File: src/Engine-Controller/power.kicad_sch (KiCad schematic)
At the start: 45 parts, among them P1 EJ508A, P7 647676-2, U2 LM22672MRE-5.0_NOPB, U3 LMS8117AMP-3.3_NOPB, U6 TPS2115APWR

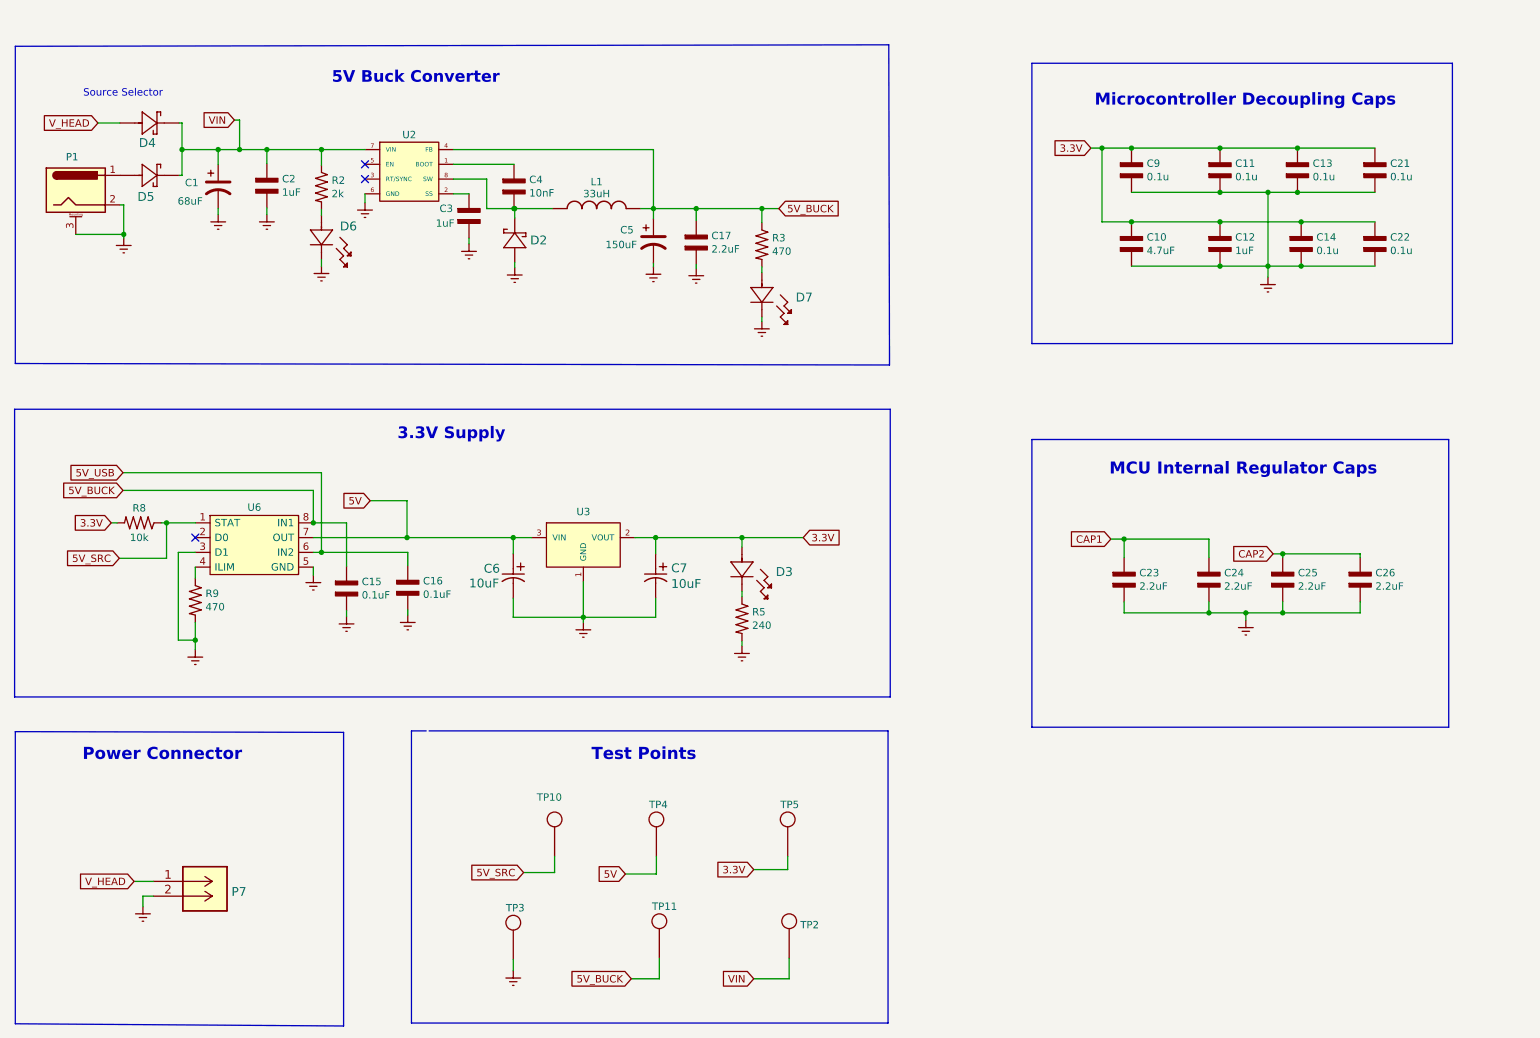
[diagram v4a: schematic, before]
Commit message: moved schematic components to 25 mil grid
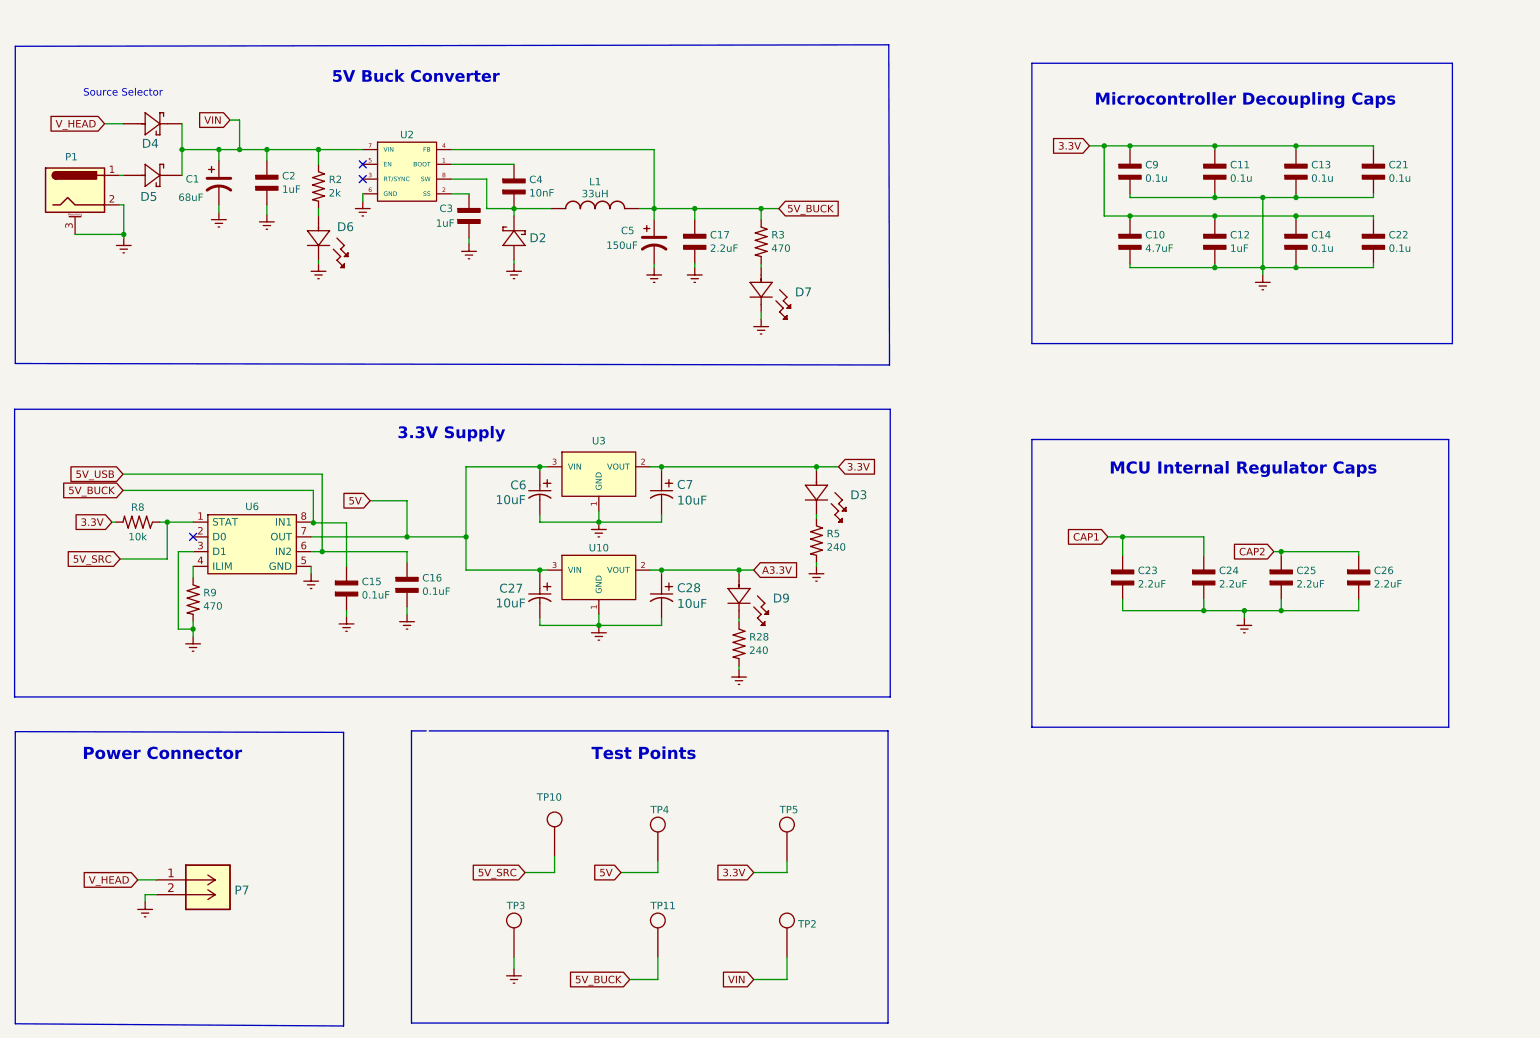
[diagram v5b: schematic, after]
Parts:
- added C27, C28: 10uF, Engine-Controller:CWR11HH106KB, symbol Engine-Controller:CWR11HH106KB
- added D9: SML-LX1206GC-TR, Engine-Controller:SML-LX1206GC-TR, symbol Engine-Controller:SML-LX1206GC-TR
- added R28: 240, Engine-Controller:RES_0603, symbol Engine-Controller:RES_0603
- added U10: LMS8117AMP-3.3_NOPB, Engine-Controller:SOT-223, symbol Engine-Controller:LMS8117AMP-3.3_NOPB
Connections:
- net 5V: now also C27.1, U10.3 (VIN)
- net Earth: now also C27.2, C28.2, R28.2, U10.1 (GND)
- new net: D9.1, R28.1
- new net A3.3V: C28.1, D9.2, U10.2 (VOUT)
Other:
- moved on the sheet: C1, C11, C12, C14, C16, C2, C24, C6, C7, D3, D4, D5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

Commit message: added schematic annotations
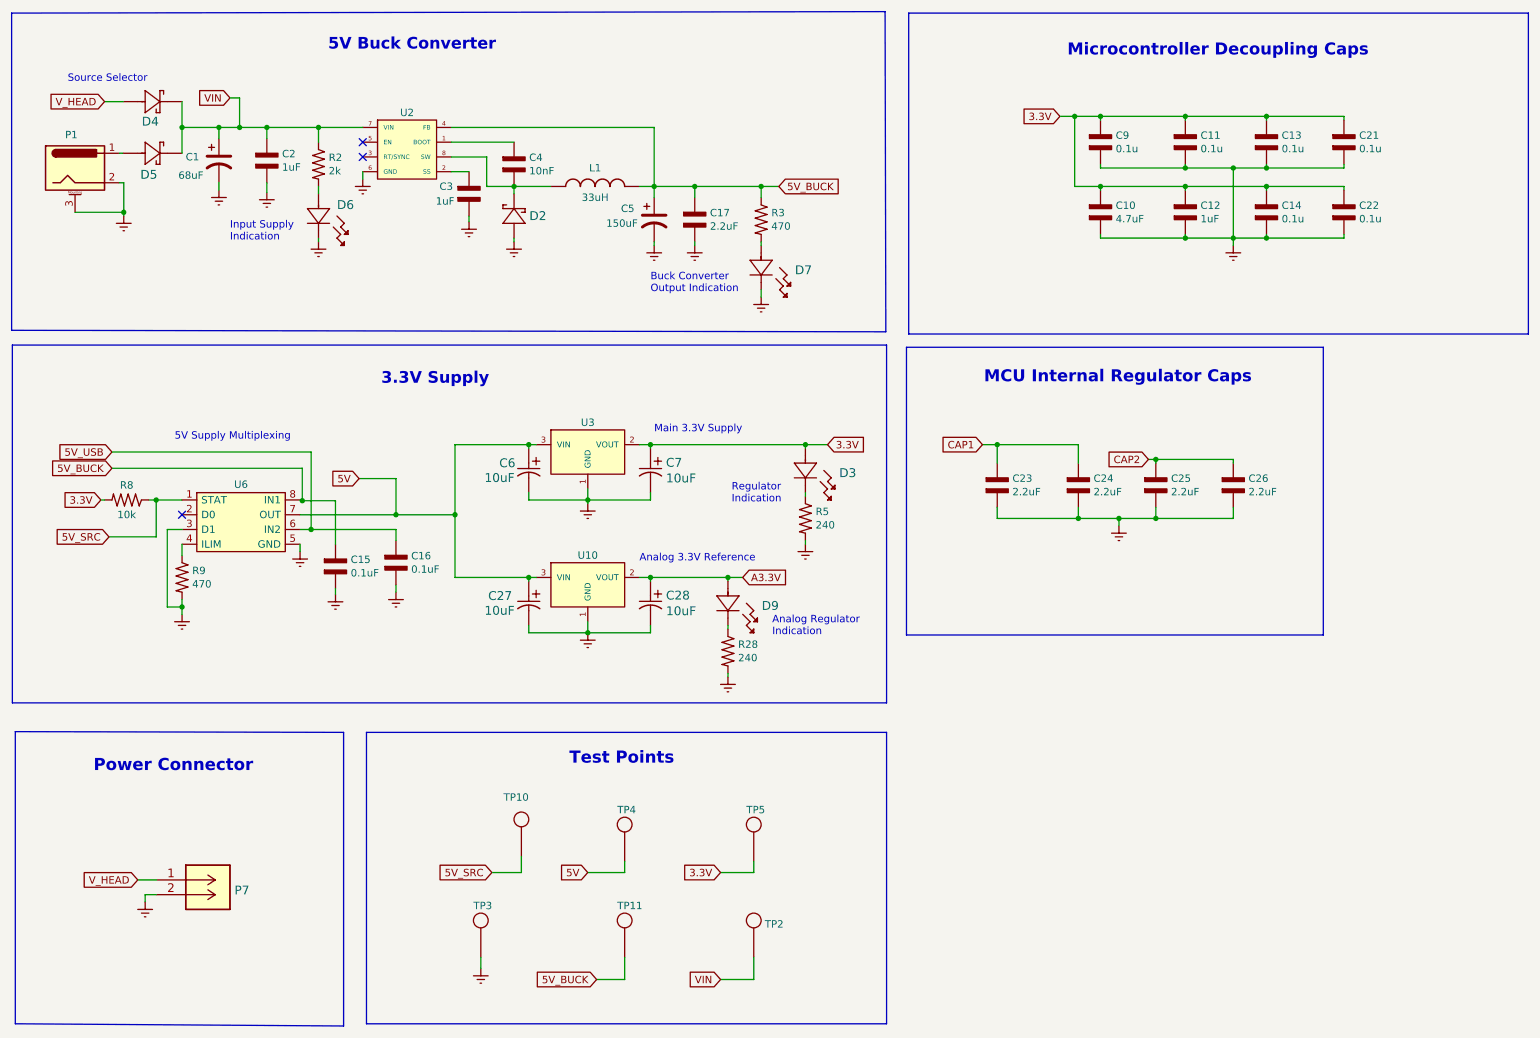
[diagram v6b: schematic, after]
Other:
- note added: "5V Supply Multiplexing"
- note added: "Analog 3.3V Reference"
- note added: "Analog Regulator Indication"
- note added: "Buck Converter Output Indication"
- note added: "Input Supply Indication"
- note added: "Main 3.3V Supply"
- note added: "Regulator Indication"
- moved on the sheet: C1, C10, C11, C12, C13, C14, C15, C16, C17, C2, C21, C22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

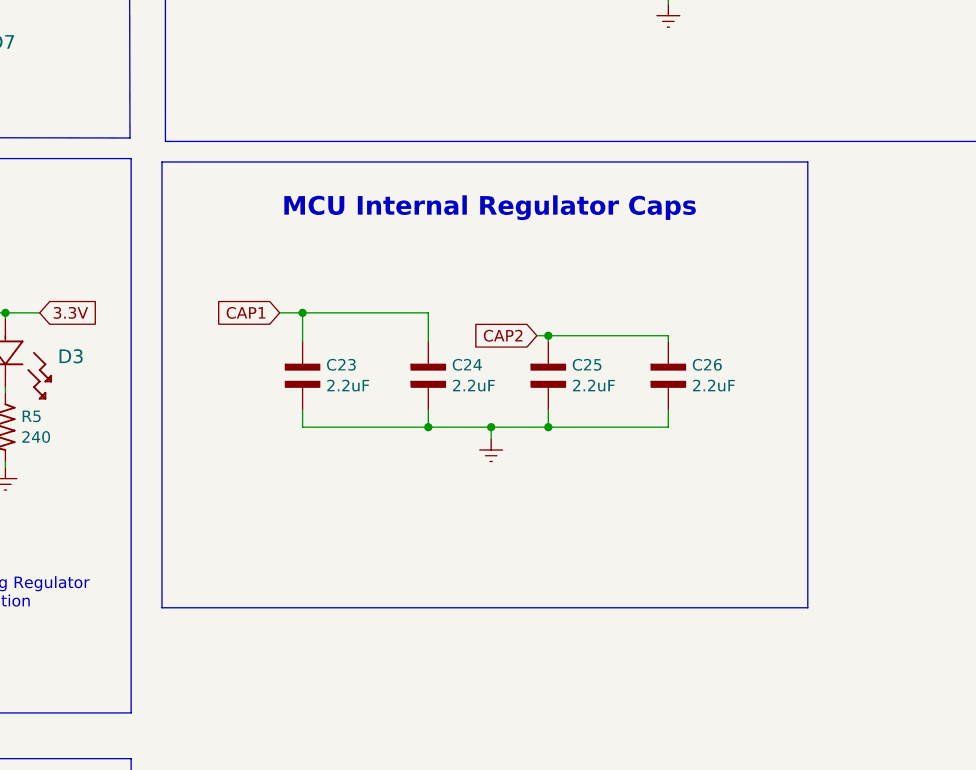
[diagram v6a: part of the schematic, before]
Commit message: added load cell amplifier to schematic
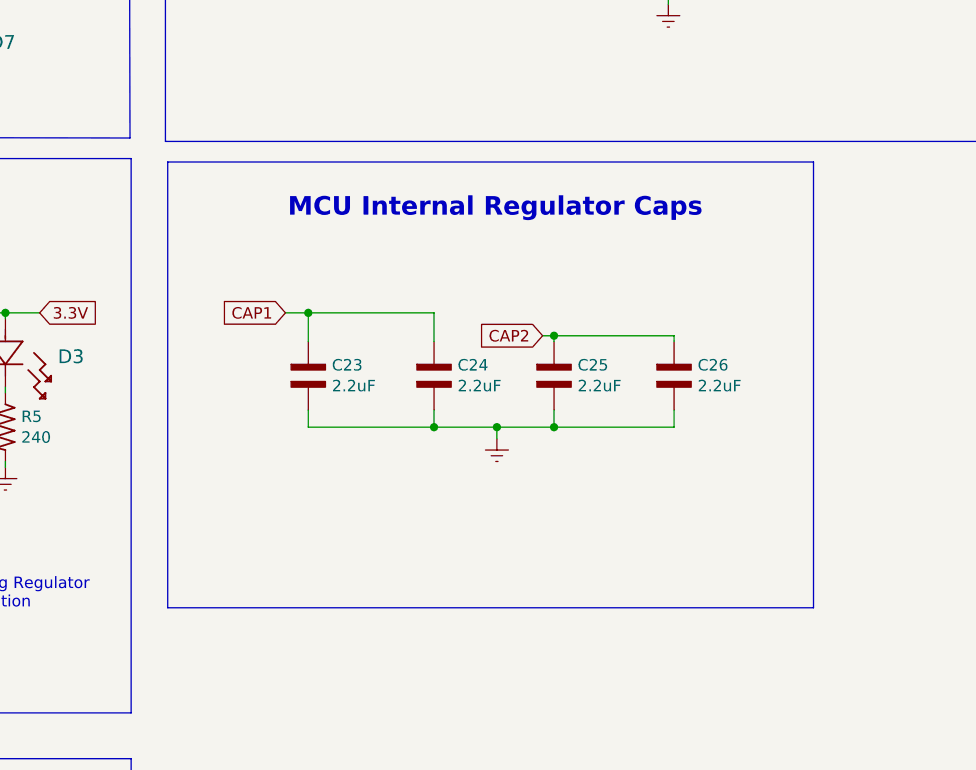
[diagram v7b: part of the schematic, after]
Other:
- moved on the sheet: C23, C24, C25, C26

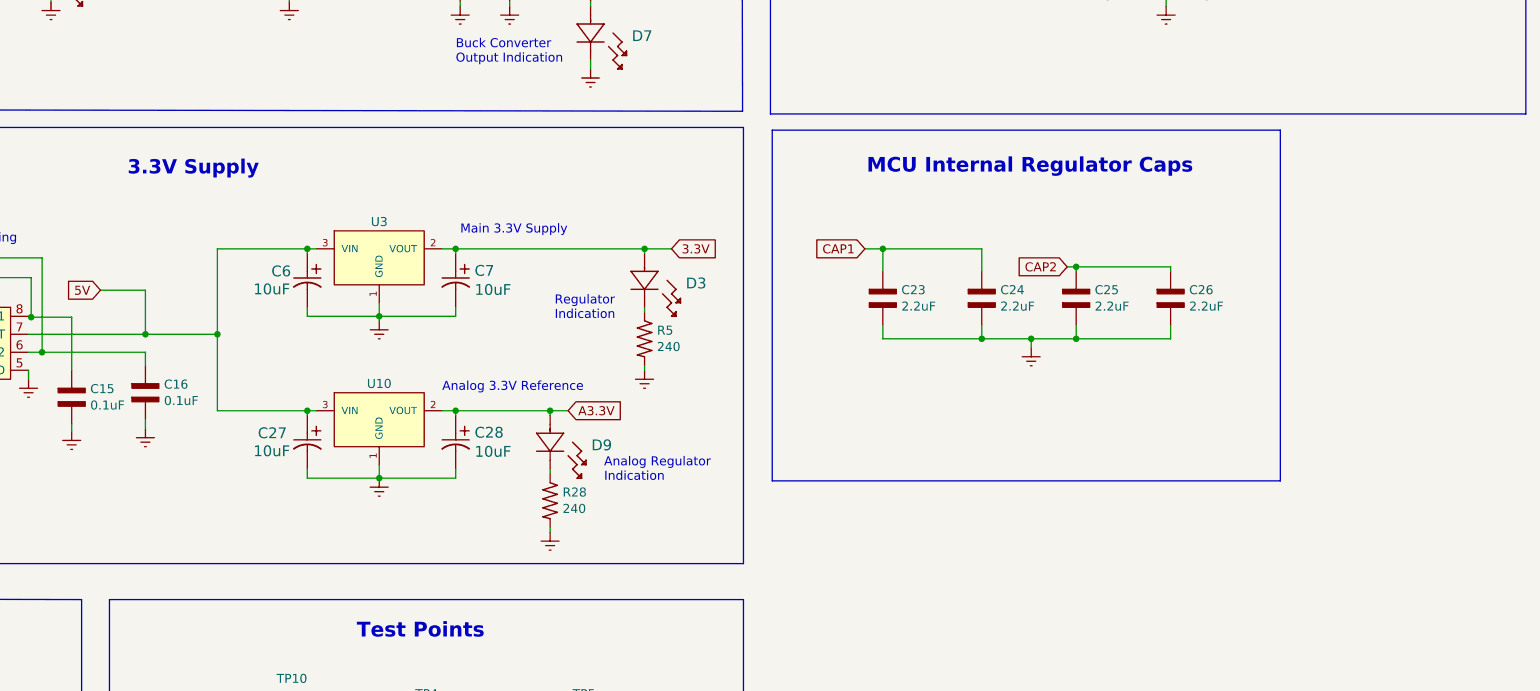
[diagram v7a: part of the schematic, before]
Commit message: added power pin header to schematic
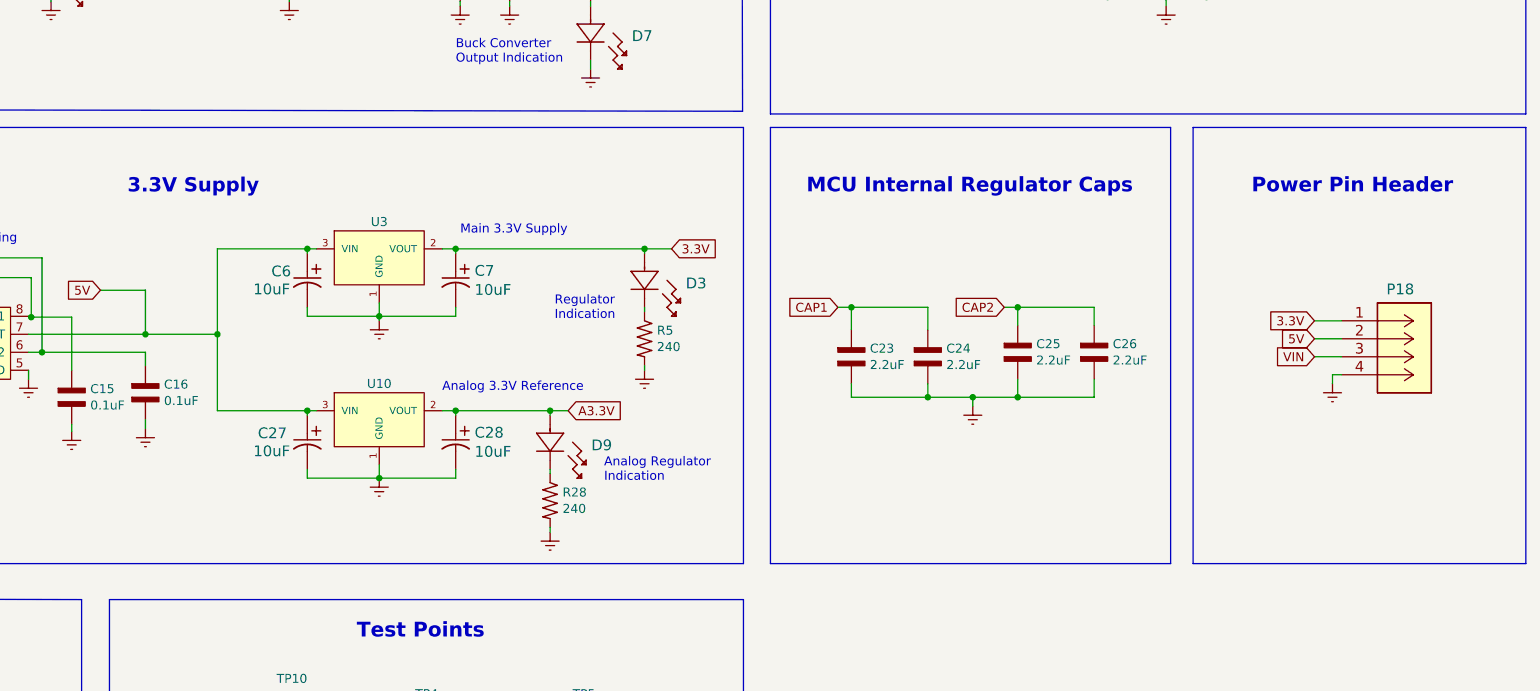
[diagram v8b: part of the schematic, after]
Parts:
- added P18: PPTC041LFBN-RC, CONN_4840.2201_SCH, symbol Engine-Controller:PPTC041LFBN-RC
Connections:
- net 3.3V: now also P18.1 (+12V)
- net 5V: now also P18.2 (GND)
- net Earth: now also P18.4
- net VIN: now also P18.3
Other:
- note added: "Power Pin Header"
- moved on the sheet: C23, C24, C25, C26
